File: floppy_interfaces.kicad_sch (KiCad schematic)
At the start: 21 parts, among them J13 Conn_01x04_Male, J14 Conn_02x17_Odd_Even, J16 Conn_01x04_Male, J6 SDF-60J for IEC 1541 serial p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, U1 74LS373, U2 74LVC374, U22 74LS06N, U3 74LVC374, U4 74LS373

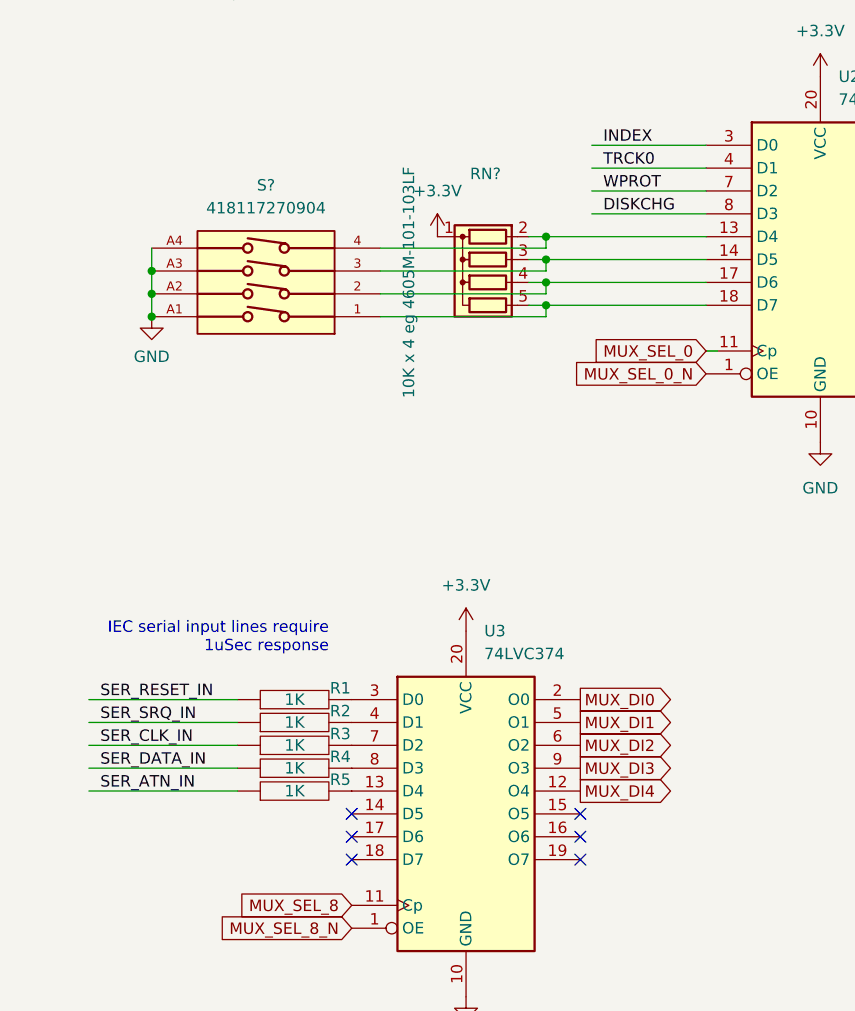
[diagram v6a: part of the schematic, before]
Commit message: relocate pins to connect RTC I2C
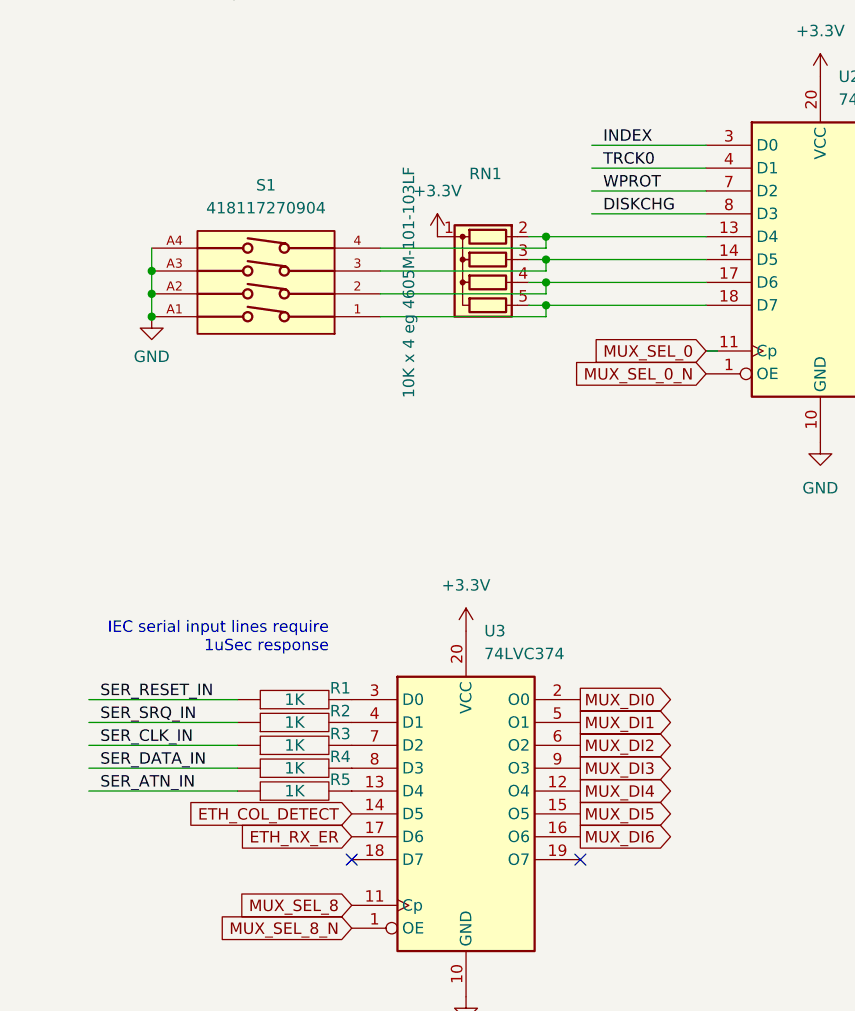
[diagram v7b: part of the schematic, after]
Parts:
- gave numbers to parts that had none: 2
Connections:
- net MUX_DI5: now also U3.15 (O5)
- net MUX_DI6: now also U3.16 (O6)
- net ETH_COL_DETECT: now reaches U3.14 (D5)
- net ETH_RX_ER: now reaches U3.17 (D6)
- no-connect marks 11 -> 7
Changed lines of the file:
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@@
   (junction (at 209.55 39.37) (diameter 0) (color 0 0 0 0)
   )
-  (no_connect (at 69.85 166.37))
   (no_connect (at 234.95 39.37))
   (no_connect (at 156.21 161.29))
@@
   (no_connect (at 156.21 166.37))
   (no_connect (at 234.95 41.91))
-  (no_connect (at 44.45 168.91))
-  (no_connect (at 69.85 168.91))
   (no_connect (at 69.85 171.45))
   (no_connect (at 156.21 168.91))
-  (no_connect (at 44.45 166.37))
   (wire (pts (xy 167.64 58.42) (xy 181.61 58.42))
     (stroke (width 0) (type default) (color 0 0 0 0))
@@
     )
   )
+  (global_label "MUX_DI6" (shape output) (at 69.85 168.91 0) (fields_autoplaced)
+    (effects (font (size 1.27 1.27)) (justify left))
+    (property "Intersheet References" "${INTERSHEET_REFS}" (id 0) (at 80.3064 168.8306 0)
+      (effects (font (size 1.27 1.27)) (justify left) hide)
+    )
+  )
   (global_label "MUX_DI0" (shape output) (at 109.22 92.075 0) (fields_autoplaced)
     (effects (font (size 1.27 1.27)) (justify left))
@@
     )
   )
+  (global_label "ETH_COL_DETECT" (shape input) (at 44.45 166.37 180) (fields_autoplaced)
+    (effects (font (size 1.27 1.27)) (justify right))
+    (property "Intersheet References" "${INTERSHEET_REFS}" (id 0) (at 26.2526 166.2906 0)
+      (effects (font (size 1.27 1.27)) (justify right) hide)
+    )
+  )
   (global_label "+12V_FUSED" (shape input) (at 217.17 104.14 0) (fields_autoplaced)
     (effects (font (size 1.27 1.27)) (justify left))
@@
     )
   )
+  (global_label "ETH_RX_ER" (shape input) (at 44.45 168.91 180) (fields_autoplaced)
+    (effects (font (size 1.27 1.27)) (justify right))
+    (property "Intersheet References" "${INTERSHEET_REFS}" (id 0) (at 31.7559 168.8306 0)
+      (effects (font (size 1.27 1.27)) (justify right) hide)
+    )
+  )
   (global_label "MUX_SEL_8" (shape input) (at 44.45 176.53 180) (fields_autoplaced)
     (effects (font (size 1.27 1.27)) (justify right))
@@
     (property "Intersheet References" "${INTERSHEET_REFS}" (id 0) (at 33.2679 36.7506 0)
       (effects (font (size 1.27 1.27)) (justify right) hide)
+    )
+  )
+  (global_label "MUX_DI5" (shape output) (at 69.85 166.37 0) (fields_autoplaced)
+    (effects (font (size 1.27 1.27)) (justify left))
+    (property "Intersheet References" "${INTERSHEET_REFS}" (id 0) (at 80.3064 166.2906 0)
+      (effects (font (size 1.27 1.27)) (justify left) hide)
     )
   )
@@
   (symbol (lib_id "00Project-DIP-SW-4:418117270904") (at 34.925 106.045 90) (unit 1)
     (in_bom yes) (on_board yes) (fields_autoplaced)
-    (property "Reference" "S?" (id 0) (at 34.925 96.52 90))
+    (property "Reference" "S1" (id 0) (at 34.925 96.52 90))
     (property "Value" "418117270904" (id 1) (at 34.925 99.06 90))
     (property "Footprint" "418117270904" (id 2) (at 34.925 106.045 0)
@@
   (symbol (lib_id "Device:R_Network04") (at 59.055 107.315 90) (mirror x) (unit 1)
     (in_bom yes) (on_board yes)
-    (property "Reference" "RN?" (id 0) (at 59.309 95.25 90))
+    (property "Reference" "RN1" (id 0) (at 59.309 95.25 90))
     (property "Value" "10K x 4 eg 4605M-101-103LF" (id 1) (at 50.8 107.315 0))
     (property "Footprint" "Resistor_THT:R_Array_SIP5" (id 2) (at 59.055 114.3 90)
@@
   (symbol (lib_id "power:+3.3V") (at 53.975 102.235 0) (mirror y) (unit 1)
     (in_bom yes) (on_board yes) (fields_autoplaced)
-    (property "Reference" "#PWR?" (id 0) (at 53.975 106.045 0)
+    (property "Reference" "#PWR0153" (id 0) (at 53.975 106.045 0)
       (effects (font (size 1.27 1.27)) hide)
     )
@@
   (symbol (lib_id "power:GND") (at 22.225 111.125 0) (unit 1)
     (in_bom yes) (on_board yes) (fields_autoplaced)
-    (property "Reference" "#PWR?" (id 0) (at 22.225 117.475 0)
-      (effects (font (size 1.27 1.27)) hide)
-    )
+    (property "Reference" "#PWR0154" (id 0) (at 22.225 117.475 0)
+      (effects (font (size 1.27 1.27)) hide)
+    )

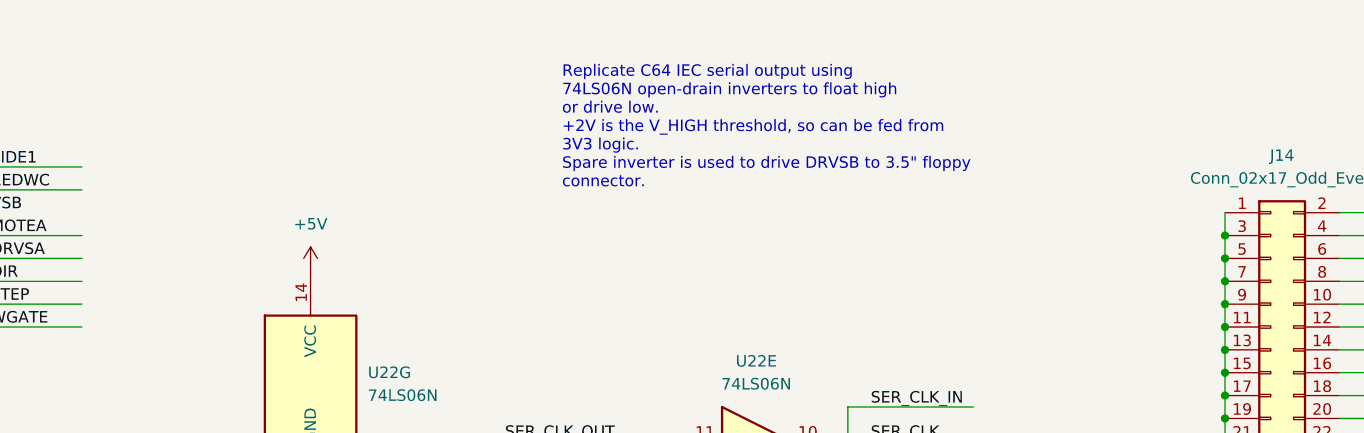
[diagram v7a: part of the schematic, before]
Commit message: add symbol and footprint for mini-DIN8 for 1565
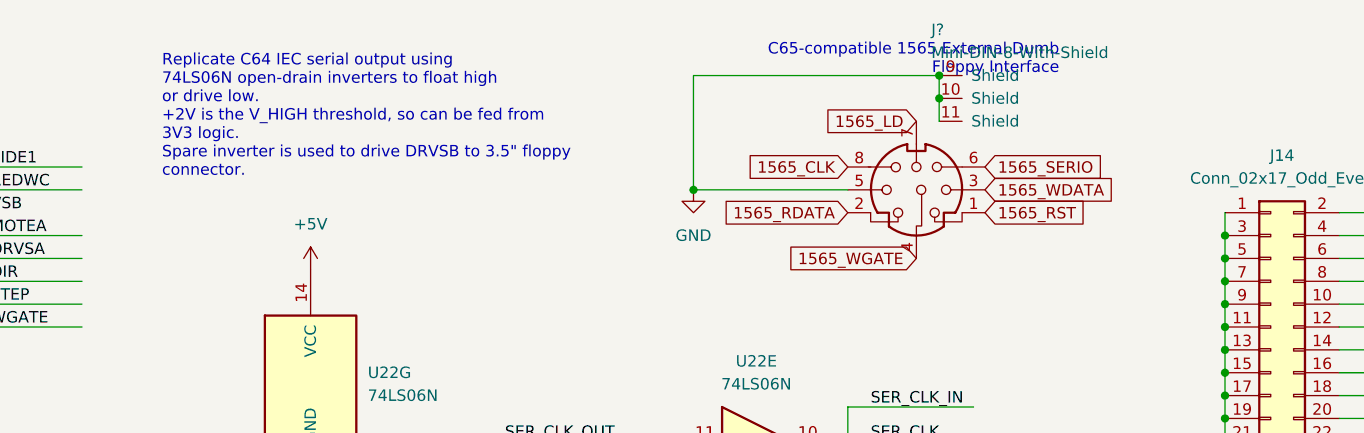
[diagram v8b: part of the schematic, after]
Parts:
- added J?: Mini-DIN-8-With-Shield, snapeda:mini-DIN-8, symbol 00Project-SDF-60J:Mini-DIN-8-With-Shield
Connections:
- net GND: now also J?.10 (Shield), J?.11 (Shield), J?.5, J?.9 (Shield)
- new net 1565_CLK: J?.8
- new net 1565_LD: J?.7
- new net 1565_RDATA: J?.2
- new net 1565_RST: J?.1
- new net 1565_SERIO: J?.6
- new net 1565_WDATA: J?.3
- new net 1565_WGATE: J?.4
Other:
- note added: "C65-compatible 1565 External Dumb Floppy Interface"
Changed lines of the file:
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@@
   (junction (at 209.55 57.15) (diameter 0) (color 0 0 0 0)
   )
+  (junction (at 150.495 34.29) (diameter 0) (color 0 0 0 0)
+  )
   (junction (at 209.55 64.77) (diameter 0) (color 0 0 0 0)
   )
+  (junction (at 177.8 21.59) (diameter 0) (color 0 0 0 0)
+  )
   (junction (at 167.64 96.52) (diameter 0) (color 0 0 0 0)
   )
@@
   )
   (junction (at 209.55 62.23) (diameter 0) (color 0 0 0 0)
+  )
+  (junction (at 177.8 24.13) (diameter 0) (color 0 0 0 0)
   )
   (junction (at 66.04 102.235) (diameter 0) (color 0 0 0 0)
@@
     (stroke (width 0) (type default) (color 0 0 0 0))
   )
+  (wire (pts (xy 177.8 24.13) (xy 177.8 21.59))
+    (stroke (width 0) (type default) (color 0 0 0 0))
+  )
   (wire (pts (xy 209.55 67.31) (xy 209.55 69.85))
     (stroke (width 0) (type default) (color 0 0 0 0))
@@
     (stroke (width 0) (type default) (color 0 0 0 0))
   )
+  (wire (pts (xy 150.495 34.29) (xy 167.64 34.29))
+    (stroke (width 0) (type default) (color 0 0 0 0))
+  )
   (wire (pts (xy 64.135 109.855) (xy 66.04 109.855))
     (stroke (width 0) (type default) (color 0 0 0 0))
@@
     (stroke (width 0) (type default) (color 0 0 0 0))
   )
+  (wire (pts (xy 177.8 21.59) (xy 150.495 21.59))
+    (stroke (width 0) (type default) (color 0 0 0 0))
+  )
   (wire (pts (xy 69.85 41.91) (xy 82.55 41.91))
     (stroke (width 0) (type default) (color 0 0 0 0))
@@
     (stroke (width 0) (type default) (color 0 0 0 0))
   )
+  (wire (pts (xy 150.495 21.59) (xy 150.495 34.29))
+    (stroke (width 0) (type default) (color 0 0 0 0))
+  )
   (wire (pts (xy 47.625 106.045) (xy 66.04 106.045))
     (stroke (width 0) (type default) (color 0 0 0 0))
@@
   )
   (wire (pts (xy 71.12 97.155) (xy 83.82 97.155))
+    (stroke (width 0) (type default) (color 0 0 0 0))
+  )
+  (wire (pts (xy 177.8 26.67) (xy 177.8 24.13))
     (stroke (width 0) (type default) (color 0 0 0 0))
   )
@@
   )
   (text "Replicate C64 IEC serial output using\n74LS06N open-drain inverters to float high\nor drive low.  \n+2V is the V_HIGH threshold, so can be fed from\n3V3 logic.\nSpare inverter is used to drive DRVSB to 3.5\" floppy\nconnector."
-    (at 135.89 34.29 0)
+    (at 91.44 33.02 0)
     (effects (font (size 1.27 1.27)) (justify left bottom))
   )
@@
   (text "ATN line is also connected to user port" (at 161.29 100.33 0)
     (effects (font (size 1.27 1.27)) (justify left bottom))
+  )
+  (text "C65-compatible 1565 External Dumb\nFloppy Interface"
+    (at 191.135 21.59 0)
+    (effects (font (size 1.27 1.27)) (justify right bottom))
   )
   (label "SER_ATN" (at 170.18 96.52 0)
@@
     )
   )
+  (global_label "1565_LD" (shape input) (at 175.26 26.67 180) (fields_autoplaced)
+    (effects (font (size 1.27 1.27)) (justify right))
+    (property "Intersheet References" "${INTERSHEET_REFS}" (id 0) (at 164.7431 26.5906 0)
+      (effects (font (size 1.27 1.27)) (justify right) hide)
+    )
+  )
   (global_label "MUX_SEL_8" (shape input) (at 130.81 176.53 180) (fields_autoplaced)
     (effects (font (size 1.27 1.27)) (justify right))
@@
     )
   )
+  (global_label "1565_SERIO" (shape input) (at 182.88 31.75 0) (fields_autoplaced)
+    (effects (font (size 1.27 1.27)) (justify left))
+    (property "Intersheet References" "${INTERSHEET_REFS}" (id 0) (at 196.6626 31.6706 0)
+      (effects (font (size 1.27 1.27)) (justify left) hide)
+    )
+  )
   (global_label "MUX_DO3" (shape input) (at 130.81 161.29 180) (fields_autoplaced)
     (effects (font (size 1.27 1.27)) (justify right))
@@
     )
   )
+  (global_label "1565_RST" (shape input) (at 182.88 36.83 0) (fields_autoplaced)
+    (effects (font (size 1.27 1.27)) (justify left))
+    (property "Intersheet References" "${INTERSHEET_REFS}" (id 0) (at 194.546 36.7506 0)
+      (effects (font (size 1.27 1.27)) (justify left) hide)
+    )
+  )
+  (global_label "1565_WDATA" (shape input) (at 182.88 34.29 0) (fields_autoplaced)
+    (effects (font (size 1.27 1.27)) (justify left))
+    (property "Intersheet References" "${INTERSHEET_REFS}" (id 0) (at 196.965 34.2106 0)
+      (effects (font (size 1.27 1.27)) (justify left) hide)
+    )
+  )
   (global_label "MUX_DO5" (shape input) (at 44.45 44.45 180) (fields_autoplaced)
     (effects (font (size 1.27 1.27)) (justify right))
@@
     (effects (font (size 1.27 1.27)) (justify right))
     (property "Intersheet References" "${INTERSHEET_REFS}" (id 0) (at 33.2679 39.2906 0)
+      (effects (font (size 1.27 1.27)) (justify right) hide)
+    )
+  )
+  (global_label "1565_WGATE" (shape input) (at 175.26 41.91 180) (fields_autoplaced)
+    (effects (font (size 1.27 1.27)) (justify right))
+    (property "Intersheet References" "${INTERSHEET_REFS}" (id 0) (at 161.1145 41.8306 0)
       (effects (font (size 1.27 1.27)) (justify right) hide)
     )
@@
     )
   )
+  (global_label "1565_CLK" (shape input) (at 167.64 31.75 180) (fields_autoplaced)
+    (effects (font (size 1.27 1.27)) (justify right))
+    (property "Intersheet References" "${INTERSHEET_REFS}" (id 0) (at 155.8531 31.6706 0)
+      (effects (font (size 1.27 1.27)) (justify right) hide)
+    )
+  )
   (global_label "FL_RDATA" (shape input) (at 239.395 74.295 0) (fields_autoplaced)
     (effects (font (size 1.27 1.27)) (justify left))
@@
     (property "Intersheet References" "${INTERSHEET_REFS}" (id 0) (at 80.3064 161.2106 0)
       (effects (font (size 1.27 1.27)) (justify left) hide)
+    )
+  )
+  (global_label "1565_RDATA" (shape input) (at 167.64 36.83 180) (fields_autoplaced)
+    (effects (font (size 1.27 1.27)) (justify right))
+    (property "Intersheet References" "${INTERSHEET_REFS}" (id 0) (at 153.7364 36.7506 0)
+      (effects (font (size 1.27 1.27)) (justify right) hide)
     )
   )
@@
     (pin "5")
   )
+  (symbol (lib_id "power:GND") (at 150.495 34.29 0) (unit 1)
+    (in_bom yes) (on_board yes) (fields_autoplaced)
+    (property "Reference" "#PWR?" (id 0) (at 150.495 40.64 0)
+      (effects (font (size 1.27 1.27)) hide)
+    )
+    (property "Value" "GND" (id 1) (at 150.495 39.37 0))
+    (property "Footprint" "" (id 2) (at 150.495 34.29 0)
+      (effects (font (size 1.27 1.27)) hide)
+    )
+    (property "Datasheet" "" (id 3) (at 150.495 34.29 0)
+      (effects (font (size 1.27 1.27)) hide)
+    )
+    (pin "1")
+  )
   (symbol (lib_id "power:+5V") (at 267.97 111.76 0) (unit 1)
     (in_bom yes) (on_board yes) (fields_autoplaced)
@@
     (pin "2")
   )
+  (symbol (lib_id "00Project-SDF-60J:Mini-DIN-8-With-Shield") (at 175.26 34.29 0) (unit 1)
+    (in_bom yes) (on_board yes) (fields_autoplaced)
+    (property "Reference" "J?" (id 0) (at 176.9111 16.51 0)
+      (effects (font (size 1.27 1.27)) (justify left))
+    )
+    (property "Value" "Mini-DIN-8-With-Shield" (id 1) (at 176.9111 19.05 0)
+      (effects (font (size 1.27 1.27)) (justify left))
+    )
+    (property "Footprint" "snapeda:mini-DIN-8" (id 2) (at 175.006 34.544 90)
+      (effects (font (size 1.27 1.27)) hide)
+    )
+    (property "Datasheet" "http://service.powerdynamics.com/ec/Catalog17/Section%2011.pdf" (id 3) (at 175.006 34.544 90)
+      (effects (font (size 1.27 1.27)) hide)
+    )
+    (pin "1")
+    (pin "10")
+    (pin "11")
+    (pin "2")
+    (pin "3")
+    (pin "4")
+    (pin "5")
+    (pin "6")
+    (pin "7")
+    (pin "8")
+    (pin "9")
+  )
   (symbol (lib_id "pspice:R") (at 38.1 161.29 90) (unit 1)
